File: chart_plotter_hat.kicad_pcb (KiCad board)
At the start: 4 copper layers, 65 x 56 mm, 57 parts, among them J1 JST PH, J10 JST PH, J2 JST PH, J3 40HAT, J4 JST PH, J5 JST PH, J6 JST PH, J7 JST PH, J8 Conn_02x03_Odd_Even, J9 JST PH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

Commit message: Updated README
Created pdf of schematic, updated board graphic
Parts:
- R11, R13, R16: value 10K -> 6.8K
- moved U6 1.45 mm to (101.3, 101.1)
- moved Y1 1.35 mm to (102.2, 111.7)
- moved C17 1.18 mm to (102.8, 115.0)
- moved C16 1.01 mm to (99.1, 114.9)
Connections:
- net CS renamed AVR_CS
- net LED_ACTION renamed LED1
- C10 pad 2: GND2 -> GND
- C15 pad 2: GND2 -> GND
- C9 pad 2: GND2 -> GND
- U1 pad 1: (no net) -> GND
- U1 pad 9: (no net) -> CAN_EN
- U7 pad 2: GND2 -> GND
- U7 pad 8: GND2 -> GND
- U8 pad 4: GND2 -> GND
- U8 pad 5: EN -> CAN_EN
- U8 pad 7: GND2 -> GND
- U9 pad 5: GND2 -> GND
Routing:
- net CAN_EN: track 0.00 -> 39.4 mm, vias 0 -> 2
- net EN: track 61.4 -> 34.0 mm, vias 3 -> 2
- net GND: track 49.1 -> 69.6 mm, vias 10 -> 11
- net Net-(U7-Pad1): track 7.04 -> 14.8 mm, vias 0 -> 2
- net VEE: track 143.7 -> 147.1 mm, vias 7 -> 8
- net +5VP: track 21.3 -> 23.9 mm, vias 0 -> 2
- net CAN_SI: track 61.8 -> 59.9 mm
- net /12VBAT: track 87.6 -> 89.4 mm
- net CAN_RST: track 56.4 -> 54.6 mm
- net CAN_INT: track 53.7 -> 52.3 mm
- net Net-(U7-Pad4): track 5.56 -> 6.64 mm
- net CAN_SO: track 49.9 -> 48.9 mm
- net CAN_SCK: track 55.4 -> 54.8 mm
- net Net-(U6-Pad2): track 8.56 -> 9.21 mm
- net Net-(U6-Pad1): track 10.6 -> 11.2 mm
- removed copper zone on F.Cu, net GND2

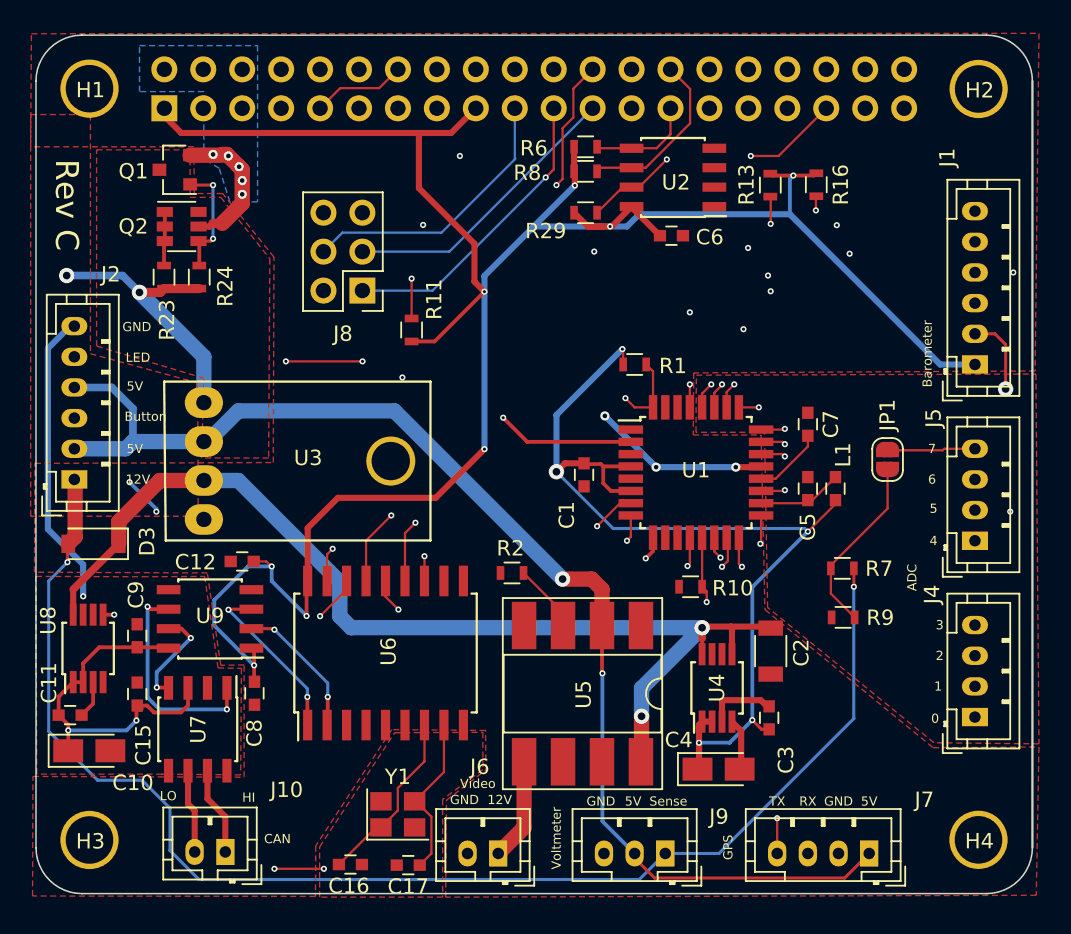
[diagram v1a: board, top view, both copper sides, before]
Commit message: Added power isolation to CAN
TVS added to CAN output
DCP01B used for power isolation from board
Another LT1762 used for CAN isolation power
Removed pull-ups from CAN controller, should be controlled by Pi
Added LED's for hat pwr, pi pwr, CAN isolation pwr, and CAN Rx
Reordered connections on Power connector
Added CAN gnd isolation pin on CAN connector
No more CAN_EN, as it is covered by isolation hookup
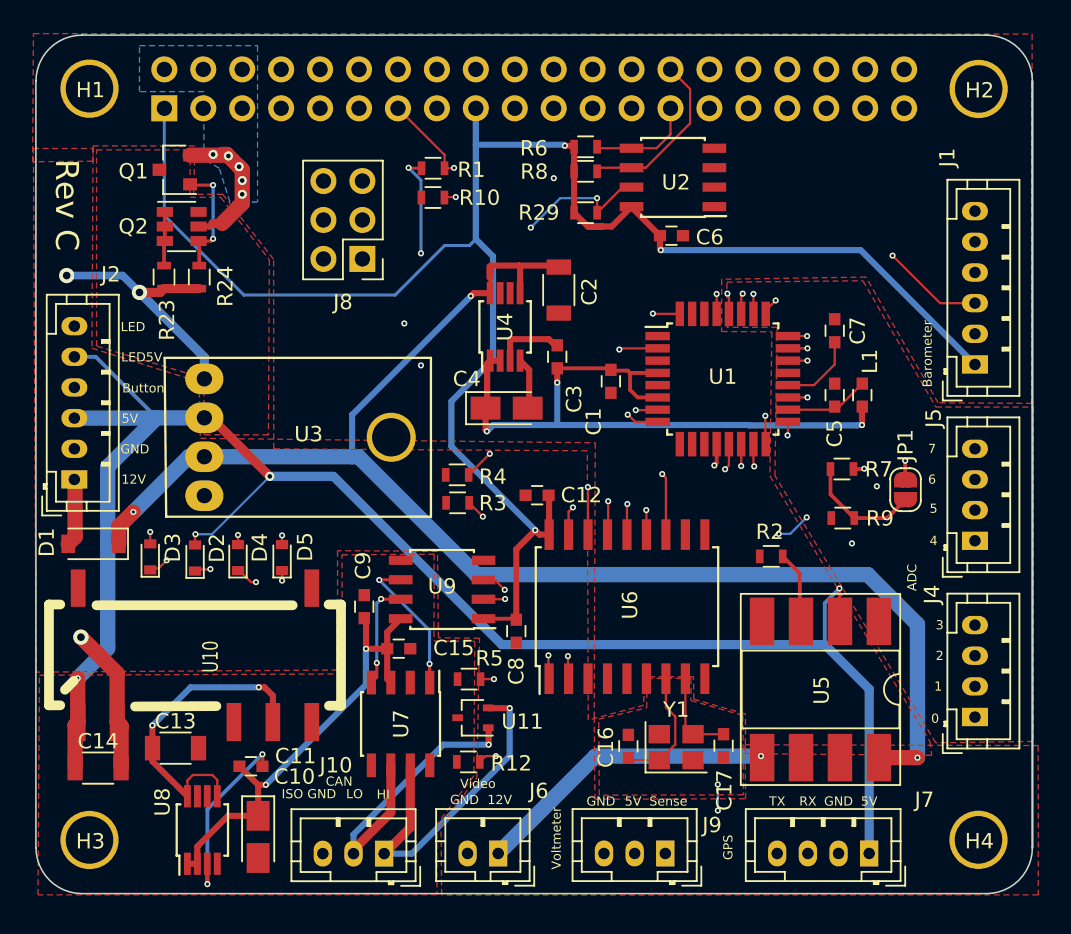
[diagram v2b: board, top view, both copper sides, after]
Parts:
- removed R11, R13, R16: 6.8K, Resistors_SMD:R_0603
- added C13: 1uF, Capacitors_SMD:C_1206, F.Cu at (87.7, 107.3)
- added C14: 2.2uF, Capacitors_SMD:C_1206, F.Cu at (82.6, 108.6)
- added D2: RED, Diodes_SMD:D_0603, F.Cu at (88.9, 94.9)
- added D3: RED, Diodes_SMD:D_0603, F.Cu at (86.0, 94.8)
- added D4: RED, Diodes_SMD:D_0603, F.Cu at (91.7, 94.9)
- added D5: GRN, Diodes_SMD:D_0603, F.Cu at (94.6, 94.9)
- added R12: 300, Resistors_SMD:R_0603, F.Cu at (106.8, 108.2)
- added R3: 390, Resistors_SMD:R_0603, F.Cu at (106.0, 91.3)
- added R4: 180, Resistors_SMD:R_0603, F.Cu at (106.0, 89.5)
- added R5: 390, Resistors_SMD:R_0603, F.Cu at (106.8, 102.8)
- added U10: DCP01B, CustomComponents:DCP01B_SO_7_14, F.Cu at (88.9, 101.3)
- added U11: VCAN26A2, TO_SOT_Packages_SMD:SOT-323_SC-70, F.Cu at (107.0, 105.3)
- J10: footprint Connectors_JST:JST_PH_B2B-PH-K_02x2.00mm_Straight -> Connectors_JST:JST_PH_B3B-PH-K_03x2.00mm_Straight
- moved R10 30.5 mm to (104.4, 71.4)
- moved U4 27.3 mm to (109.2, 79.8)
- moved C3 27.3 mm to (112.5, 81.8)
- moved C4 27.3 mm to (109.2, 85.2)
- moved C2 27.3 mm to (112.7, 77.5)
- moved C17 22.0 mm to (123.4, 107.2), turned to 270 degrees
- moved C12 19.7 mm to (111.2, 90.8)
- moved C16 19.7 mm to (117.2, 107.2), turned to 90 degrees
- moved Y1 18.7 mm to (120.3, 107.3)
- moved R1 18.4 mm to (104.5, 69.5)
- moved C8 17.6 mm to (109.9, 99.7)
- moved C15 17.3 mm to (102.2, 100.8), turned to 0 degrees
- moved R2 16.9 mm to (126.5, 94.8)
- moved U6 16.0 mm to (117.1, 98.1)
- moved U5 15.5 mm to (129.7, 103.5)
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- renumbered D3 to D1
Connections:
- C10 pad 2: GND -> GND2
- C15 pad 2: GND -> GND2
- C9 pad 2: GND -> GND2
- J2 pad 2: +5V -> GND
- J2 pad 3: BUTTON -> +5V
- J2 pad 4: +5V -> BUTTON
- J2 pad 5: LED1 -> +5V
- J2 pad 6: GND -> LED1
- U1 pad 9: CAN_EN -> (no net)
- U7 pad 2: GND -> GND2
- U7 pad 8: GND -> GND2
- U8 pad 4: GND -> GND2
- U8 pad 5: CAN_EN -> Net-(C13-Pad1)
- U8 pad 7: GND -> (no net)
- U8 pad 8: +12V -> Net-(C13-Pad1)
- U9 pad 5: GND -> GND2
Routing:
- net +5V: track 81.7 -> 132.0 mm, vias 2 -> 4
- net CAN_EN: track 39.4 -> 0.00 mm, vias 2 -> 0
- net Net-(D3-Pad1): track 0.00 -> 39.0 mm, vias 0 -> 2
- net GND: track 69.6 -> 33.4 mm, vias 11 -> 7
- net A7: track 52.6 -> 16.7 mm, vias 1 -> 2
- net +3V3: track 64.5 -> 96.4 mm, vias 5 -> 7
- net VEE: track 147.1 -> 118.7 mm, vias 8 -> 3
- net A6: track 45.5 -> 17.2 mm
- net Net-(D5-Pad1): track 0.00 -> 26.5 mm, vias 0 -> 2
- net EEPROM: track 51.0 -> 26.0 mm
- net +12V: track 70.4 -> 94.0 mm, vias 2 -> 3
- net Net-(D2-Pad1): track 0.00 -> 22.8 mm, vias 0 -> 2
- net Net-(C13-Pad1): track 0.00 -> 20.7 mm, vias 0 -> 2
- net Net-(D4-Pad1): track 0.00 -> 20.5 mm, vias 0 -> 2
- net +5VP: track 23.9 -> 42.6 mm, vias 2 -> 3
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- added copper zone on F.Cu, net GND2
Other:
- board text added: "ISO GND"
- board text added: "LED5V"

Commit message: Renamed some resistors
Changed resistor value from 180 to 220, to match inventory
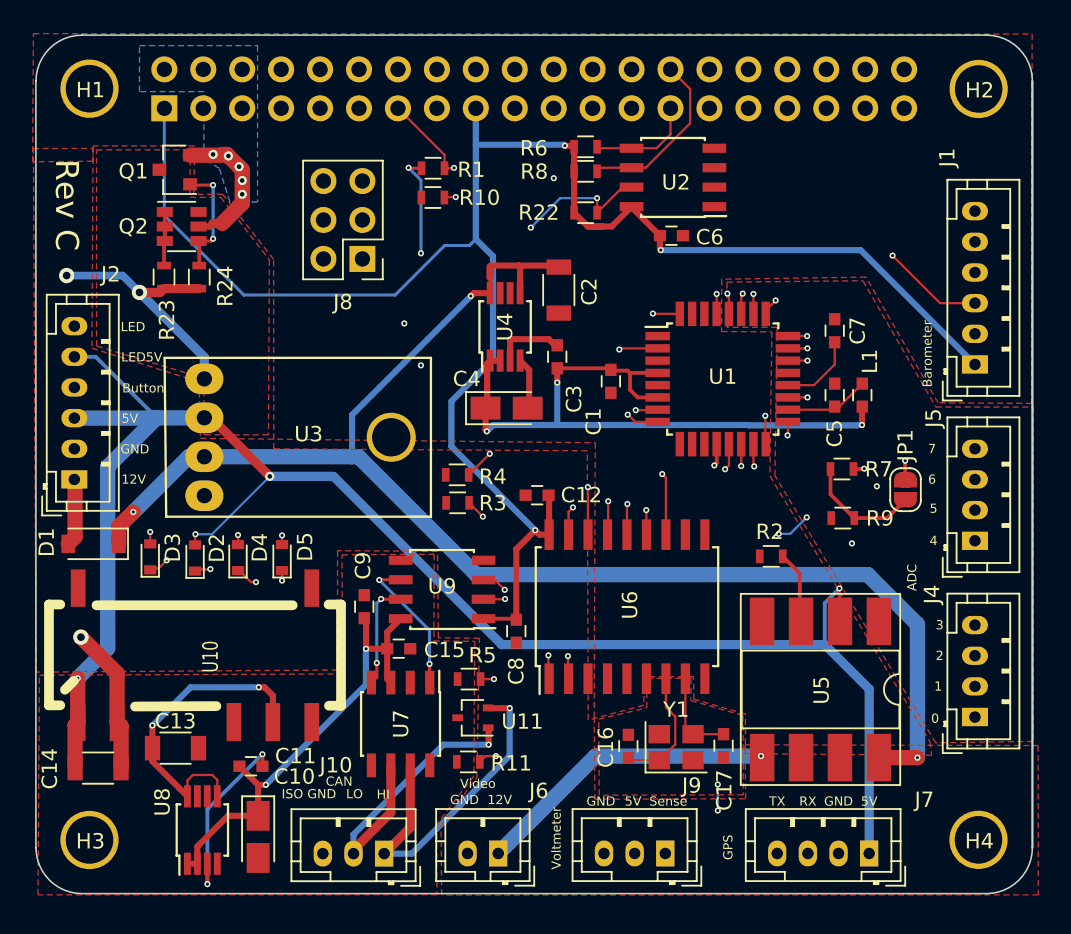
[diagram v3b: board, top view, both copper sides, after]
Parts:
- R4: value 180 -> 220
- renumbered R12 to R11, R29 to R22

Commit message: Added DS1307 RTC
Added coin cell battery holder
updated bom
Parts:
- added C18: .1uF, Capacitors_SMD:C_0603, F.Cu at (130.0, 68.2)
- added J11: Coin Battery Holder, geda:3001, B.Cu at (135.4, 76.1)
- added U12: DS1307Z+, Housings_SOIC:SOIC-8_3.9x4.9mm_Pitch1.27mm, F.Cu at (129.3, 71.8)
- added Y2: ECS-.327-6-13X, Crystals:Crystal_Round_d2.0mm_Vertical, F.Cu at (123.7, 68.9)
- U10: value DCP01B -> DCP010505BP-U
- U4: value LT1762-3.3 -> LT1762EMS8-3.3
- U8: value LT1762-MS8 -> LT1762EMS8-5
- U9: value ADuM1201BR -> ADuM1281CRZ
- moved C6 2.08 mm to (117.9, 74.0)
- moved R22 2.08 mm to (112.3, 72.5)
- moved R6 2.08 mm to (112.3, 68.2)
- moved R8 2.08 mm to (112.3, 69.8)
- moved U2 2.08 mm to (118.0, 70.2)
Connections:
- U8 pad 7: (no net) -> GND2
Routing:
- net VEE: track 118.7 -> 134.4 mm, vias 3 -> 4
- net Net-(J11-Pad2): track 0.00 -> 14.5 mm, vias 0 -> 1
- net SCL: track 64.5 -> 70.6 mm, vias 0 -> 1
- net /12VBAT: track 82.9 -> 88.7 mm
- net SDA: track 62.3 -> 67.8 mm, vias 0 -> 1
- net SerialTX: track 69.9 -> 72.9 mm
- net Net-(U12-Pad1): track 0.00 -> 2.71 mm
- net XCLR: track 45.3 -> 47.8 mm
- net Net-(U12-Pad2): track 0.00 -> 2.46 mm
- net /ID_SC_EEPROM: track 11.5 -> 13.7 mm
- net SerialRX: track 65.4 -> 67.4 mm
- net A7: track 16.7 -> 18.7 mm
- net A5: track 27.0 -> 28.6 mm
- net A3: track 30.7 -> 32.3 mm
- net A4: track 27.0 -> 28.4 mm
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
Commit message: Removed DS1307, (Not avail), added STEMMA QT conx
can connect an adafruit breakout board for RTC instead
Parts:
- removed C18: .1uF, Capacitors_SMD:C_0603
- removed U12: DS1307Z+, Housings_SOIC:SOIC-8_3.9x4.9mm_Pitch1.27mm
- removed Y2: ECS-.327-6-13X, Crystals:Crystal_Round_d2.0mm_Vertical
- J11: value Coin Battery Holder -> Qwiic; footprint geda:3001 -> Connectors_JST:JST_SH_BM04B-SRSS-TB_04x1.00mm_Straight; moved to F.Cu
- moved J11 11.0 mm to (125.5, 71.5), turned to 270 degrees
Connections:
- J11 pad 2: Net-(J11-Pad2) -> VEE
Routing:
- net Net-(J11-Pad2): track 14.5 -> 0.00 mm, vias 1 -> 0
- net VEE: track 134.4 -> 123.6 mm
- net SDA: track 67.8 -> 75.6 mm, vias 1 -> 3
- net SCL: track 70.6 -> 76.1 mm
- net Net-(U12-Pad1): track 2.71 -> 0.00 mm
- net Net-(U12-Pad2): track 2.46 -> 0.00 mm

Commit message: Removed 6 pin J1, replaced with 2 pin J1
barometer databus now goes through qwiic connector, only
interrupt lines are in J1
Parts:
- J1: footprint Connectors_JST:JST_PH_B6B-PH-K_06x2.00mm_Straight -> Connectors_JST:JST_PH_B2B-PH-K_02x2.00mm_Straight
- moved J11 15.0 mm to (140.3, 73.1)
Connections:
- J1 pad 1: VEE -> EOC
- J1 pad 2: GND -> XCLR
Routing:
- net SCL: track 76.1 -> 58.3 mm
- net SDA: track 75.6 -> 61.4 mm, vias 3 -> 1
- net EOC: track 58.0 -> 68.0 mm, vias 1 -> 0
- net VEE: track 123.6 -> 115.5 mm
- net XCLR: track 47.8 -> 49.1 mm
- net MISO: track 42.5 -> 43.3 mm
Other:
- board text added: "EOC"
- board text added: "XCLR"

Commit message: Added R12 pull-down to EN, jumper for eeprom write
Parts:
- added J12: EWRITE, Pin_Headers:Pin_Header_Straight_1x02_Pitch2.54mm, F.Cu at (124.2, 69.7)
- added R12: 1.6K, Resistors_SMD:R_0603, F.Cu at (116.7, 88.2)
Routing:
- net EEPROM: track 25.3 -> 36.1 mm
- net EN: track 33.6 -> 39.5 mm, vias 1 -> 2
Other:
- board text added: "Rev D"
- board text removed: "Rev C"

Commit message: Added pullup on CAN RST, removed jumper on EEPROM write
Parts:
- removed J12: EWRITE, Pin_Headers:Pin_Header_Straight_1x02_Pitch2.54mm
- added R13: 10K, Resistors_SMD:R_0603, F.Cu at (112.8, 89.0)
- added TP1: EEPROM Write, Measurement_Points:Measurement_Point_Square-SMD-Pad_Small, F.Cu at (109.2, 71.5)
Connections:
- J3 pad 13: BUTTON -> (no net)
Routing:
- net EEPROM: track 36.1 -> 28.3 mm
- net CAN_RST: track 44.3 -> 46.9 mm
- net VEE: track 115.5 -> 117.4 mm
- net BUTTON: track 63.9 -> 65.4 mm, vias 2 -> 3
